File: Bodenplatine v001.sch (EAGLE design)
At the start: 113 parts, among them K1 RY612012, K2 RY612012, K3 RY612012, K4 RY612012, K5 RY612012, K6 RY612012, K7 RY612012, K8 RY612012, K9 RY612012, Q1 BC846BLT1SMD, Q2 BC846BLT1SMD, Q3 BC846BLT1SMD, Q4 BC846BLT1SMD, Q5 BC846BLT1SMD, Q6 BC846BLT1SMD, Q7 BC846BLT1SMD, Q8 BC846BLT1SMD, Q9 BC846BLT1SMD, X1 SPRINGCON_AST125_5X2, X10 SPRINGCON_AST125_3X2, X11 SPRINGCON_AST125_4X2, X12 SPRINGCON_AST125_4X2, X13 SPRINGCON_AST125_5X2, X14 236-403, X15 236-402, X2 SPRINGCON_AST125_5X2, X3 SPRINGCON_AST125_5X2, X4 SPRINGCON_AST125_5X2, X5 SPRINGCON_AST125_5X2, X6 SPRINGCON_AST125_5X2, X7 SPRINGCON_AST125_5X2, X8 SPRINGCON_AST125_5X2, X9 SPRINGCON_AST125_5X2

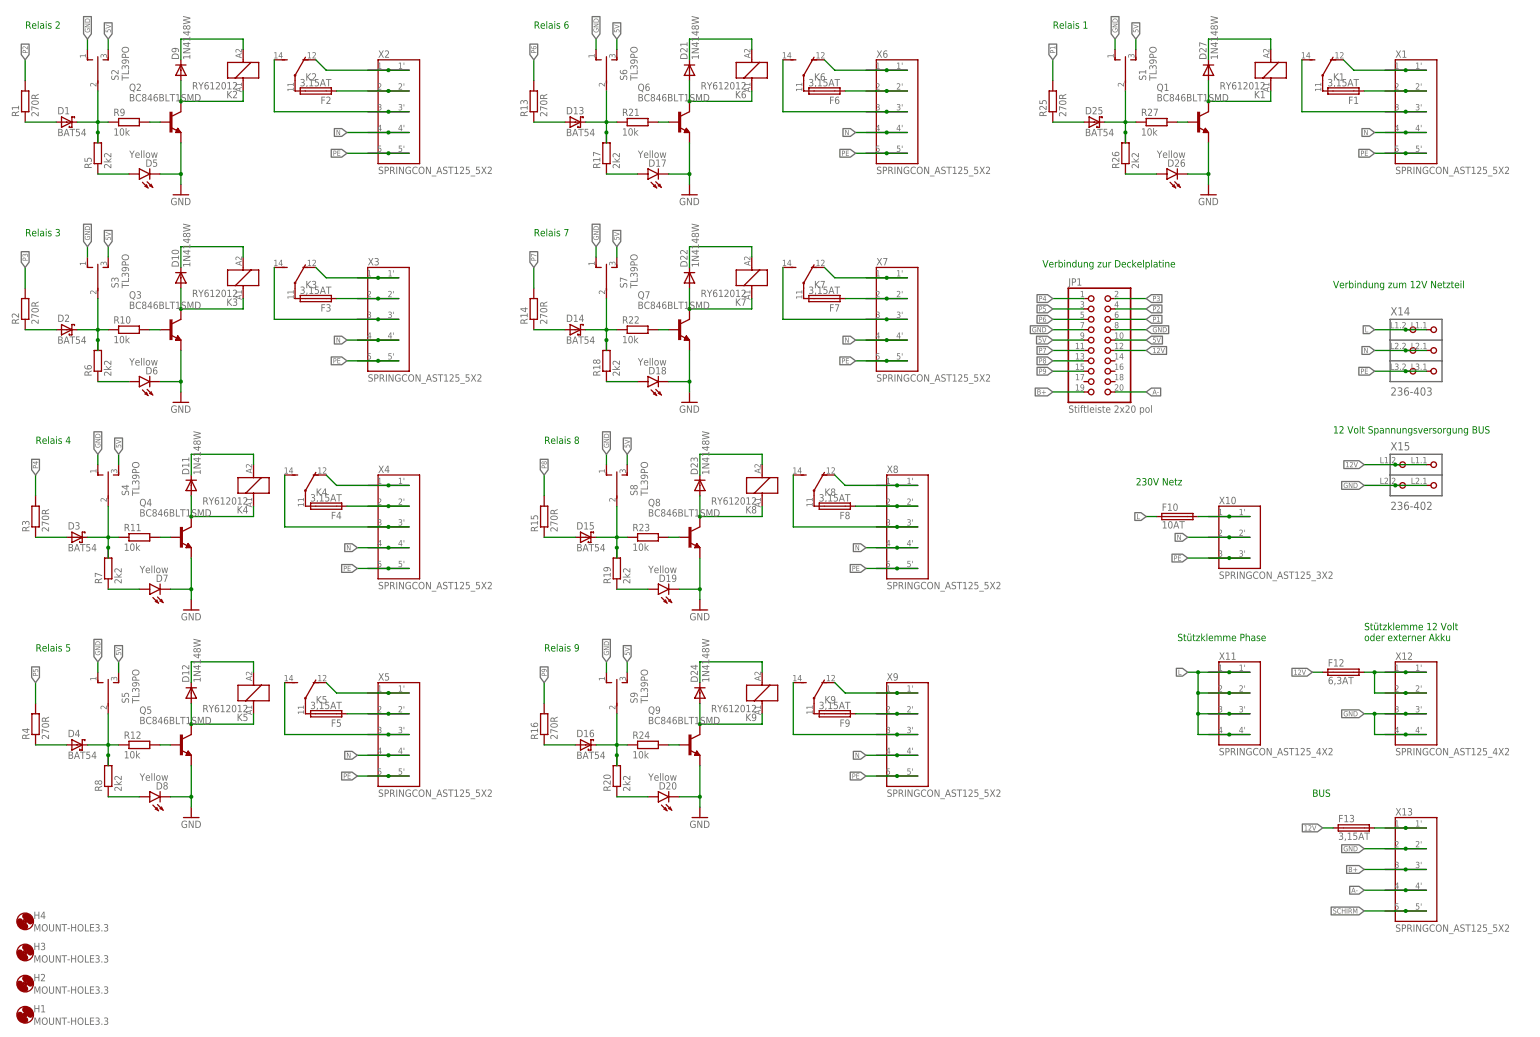
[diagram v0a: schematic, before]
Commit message: Sicherungshalter nach FPG4 ausgetauscht
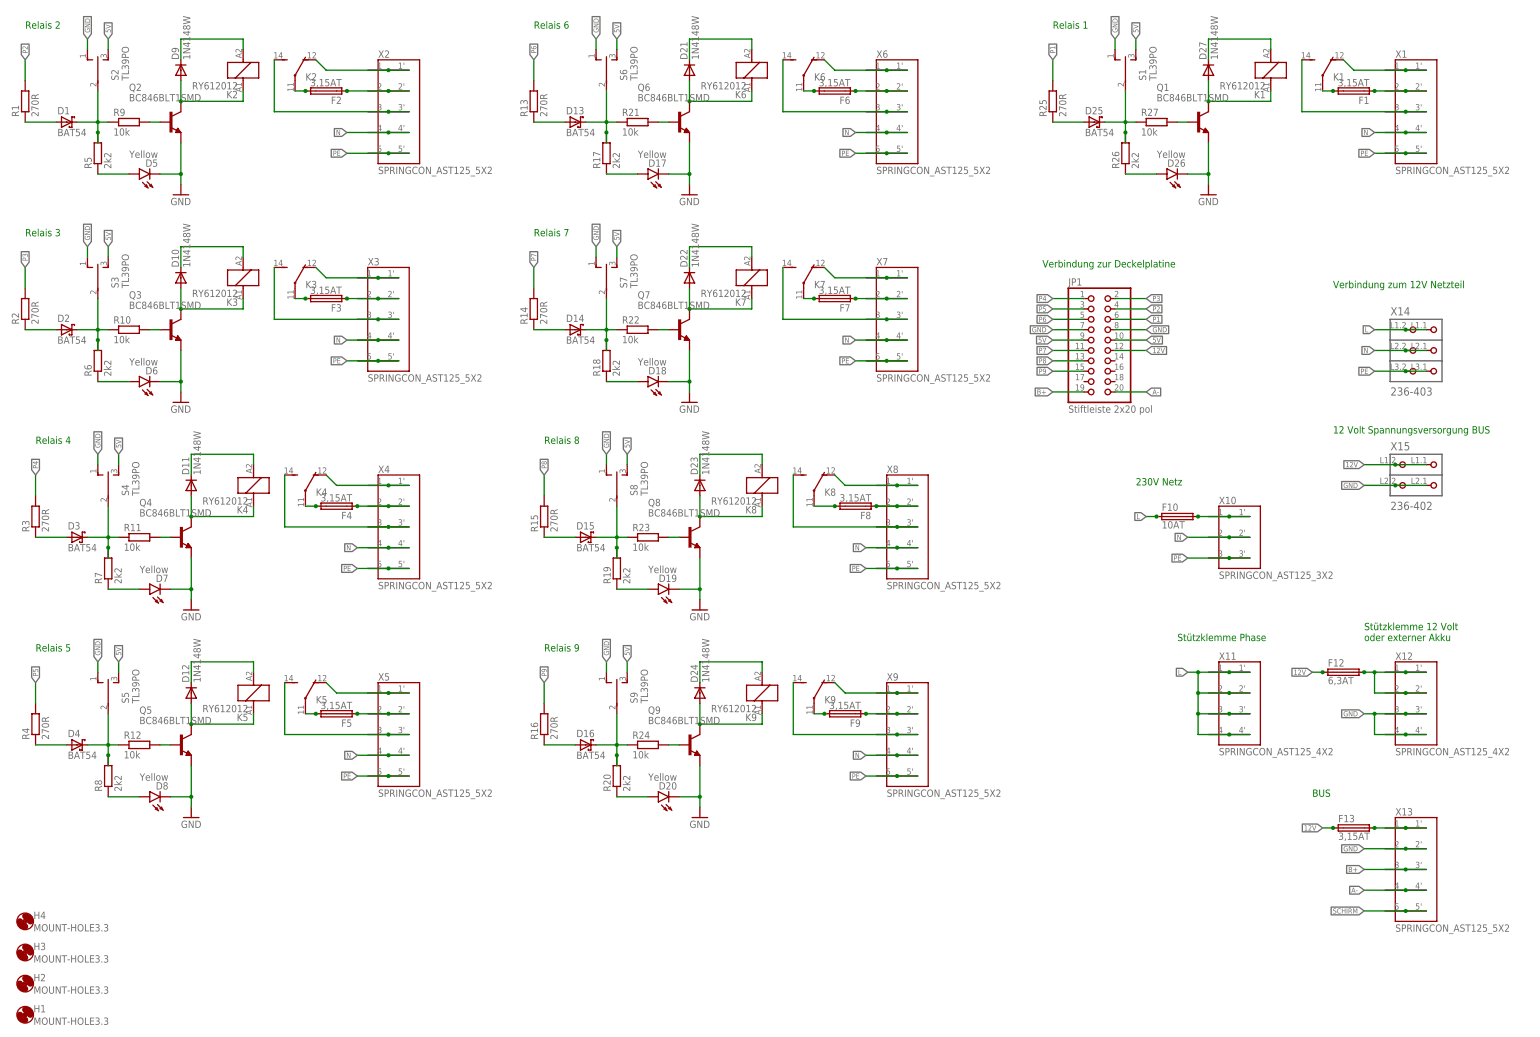
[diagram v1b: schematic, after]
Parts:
- F1, F10, F12, F13, F2, F3, F4, F5, F6, F7, F8, F9: device xMZ-Mod-Touch-Bodenplatine:F456 -> xMZ-Mod-Touch-Bodenplatine:FPG4
- Q1, Q2, Q3, Q4, Q5, Q6, Q7, Q8, Q9: MF (none) -> ON SEMICONDUCTOR; MPN (none) -> BC846BWT1G
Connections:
- net 12V: now also F12.1@2, F13.1@2
- net L: now also F10.1@2
- net N$1: now also F2.1@2
- net N$12: now also F3.2@2
- net N$19: now also F3.1@2
- net N$22: now also F4.2@2
- net N$29: now also F4.1@2
- net N$3: now also F2.2@2
- net N$32: now also F5.2@2
- net N$39: now also F5.1@2
- net N$42: now also F6.2@2
- net N$49: now also F6.1@2
- net N$52: now also F7.2@2
- net N$59: now also F7.1@2
- net N$62: now also F8.2@2
- net N$69: now also F8.1@2
- net N$72: now also F9.2@2
- net N$79: now also F9.1@2
- net N$82: now also F1.2@2
- net N$89: now also F1.1@2
- net N$91: now also F10.2@2
- net N$92: now also F13.2@2
- net N$94: now also F12.2@2

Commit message: Relais Anschlüsse A1 und A2 im Schema gedreht
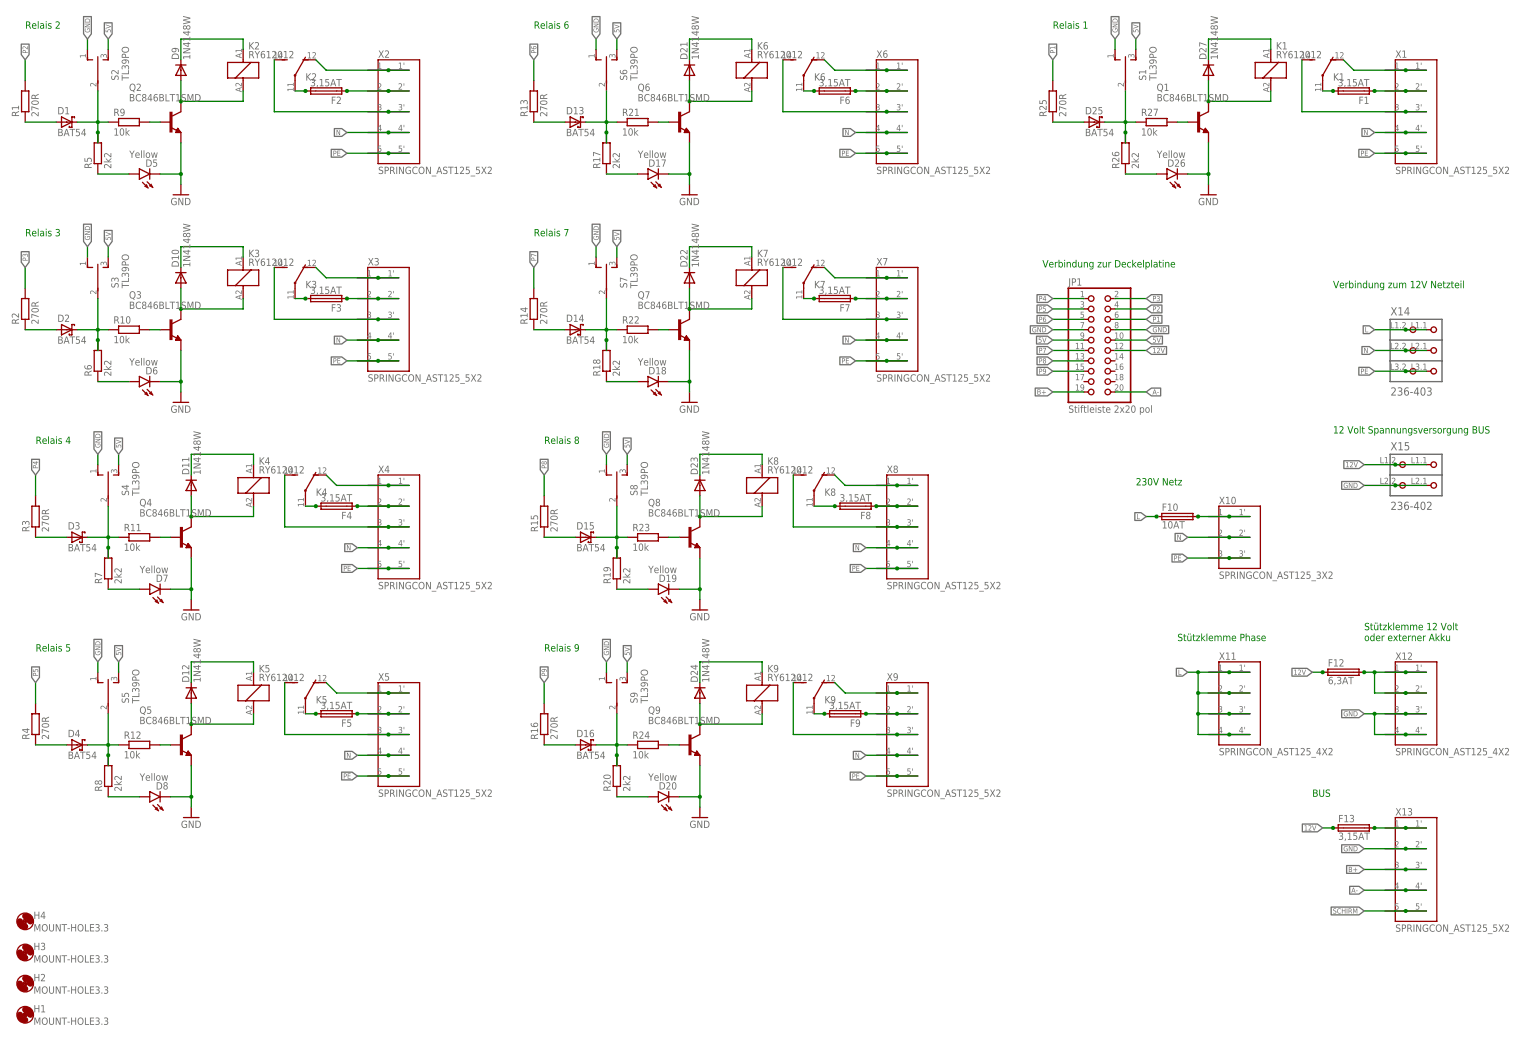
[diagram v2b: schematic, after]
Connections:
- net N$11: now also K21.1; no longer K21.2
- net N$17: now also K31.1; no longer K31.2
- net N$18: now also K31.2; no longer K31.1
- net N$27: now also K41.1; no longer K41.2
- net N$28: now also K41.2; no longer K41.1
- net N$37: now also K51.1; no longer K51.2
- net N$38: now also K51.2; no longer K51.1
- net N$47: now also K61.1; no longer K61.2
- net N$48: now also K61.2; no longer K61.1
- net N$5: now also K21.2; no longer K21.1
- net N$57: now also K71.1; no longer K71.2
- net N$58: now also K71.2; no longer K71.1
- net N$67: now also K81.1; no longer K81.2
- net N$68: now also K81.2; no longer K81.1
- net N$77: now also K91.1; no longer K91.2
- net N$78: now also K91.2; no longer K91.1
- net N$87: now also K11.1; no longer K11.2
- net N$88: now also K11.2; no longer K11.1
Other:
- moved on the sheet: K1, K2, K3, K4, K5, K6, K7, K8, K9

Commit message: Replace LL4148 Diode
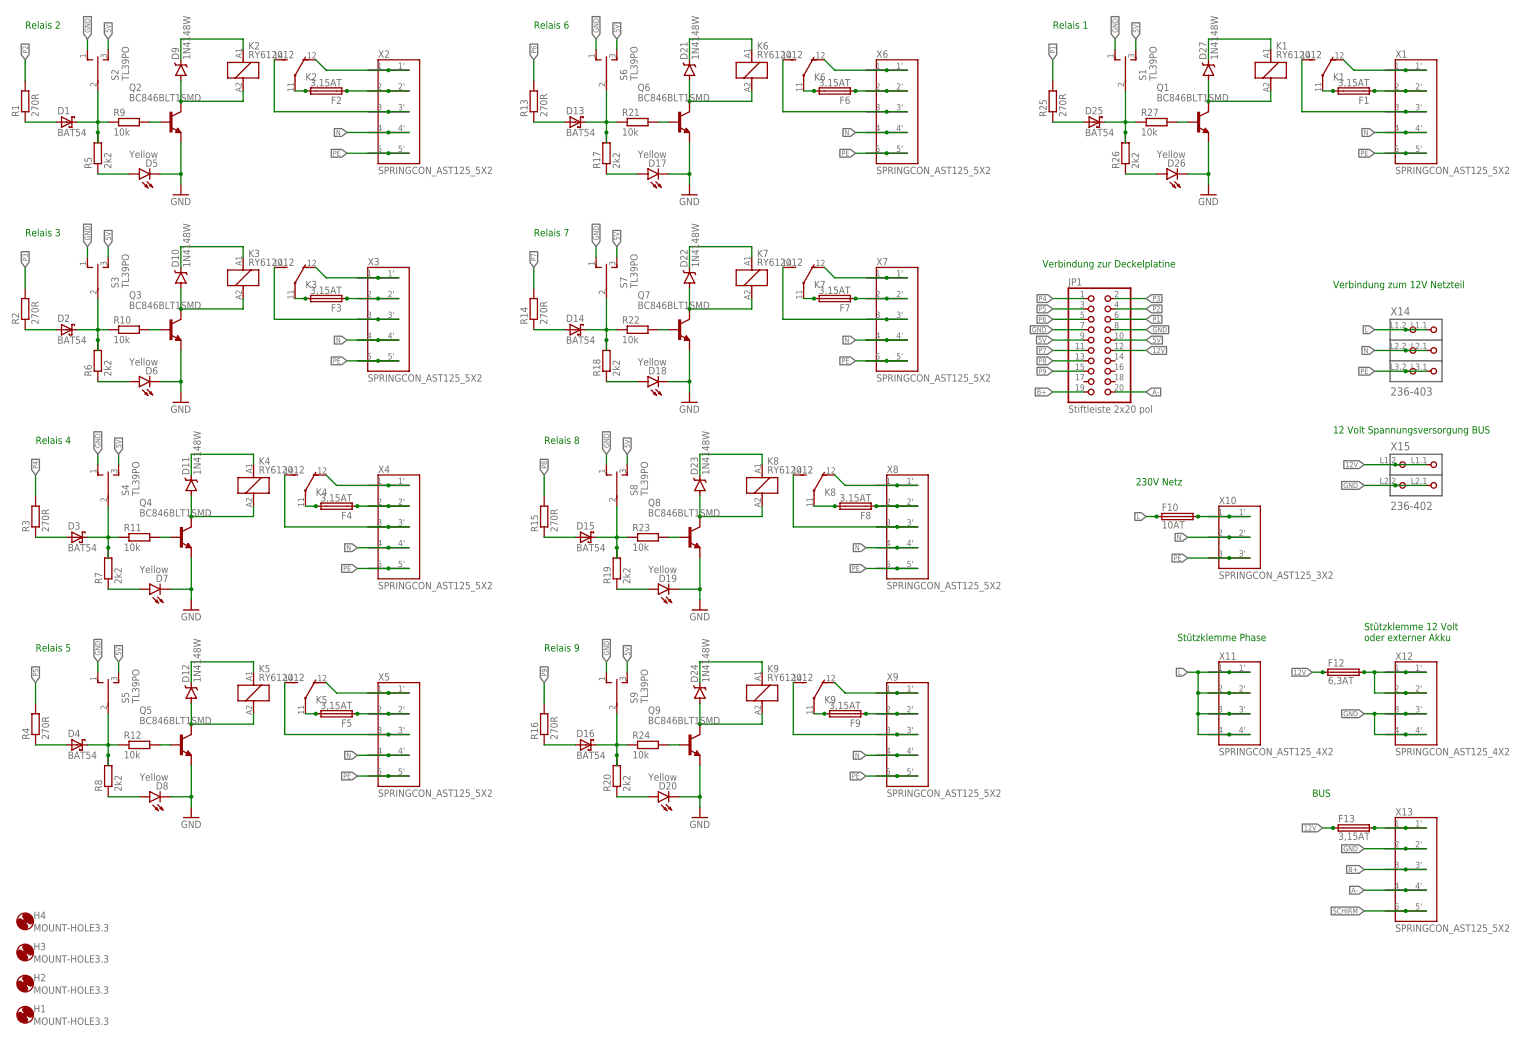
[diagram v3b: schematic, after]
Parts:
- D10, D11, D12, D21, D22, D23, D24, D27, D9: device diode:1N4148DO35-7 -> xMZ-Mod-Touch-Bodenplatine:LL4148; MF (none) -> VISHAY; MPN (none) -> LL4148-GS08; OC_FARNELL unknown -> 9549986
- F1, F10, F12, F13, F2, F3, F4, F5, F6, F7, F8, F9: OC_FARNELL (none) -> unknown
- JP1: MF (none) -> TE CONNECTIVITY / AMP; MPN (none) -> 825440-5; OC_FARNELL unknown -> 3417773
